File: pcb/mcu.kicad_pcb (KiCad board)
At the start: 2 copper layers, 40 x 27.1 mm, 11 parts, among them J700 Conn_01x20, J701 BL_CONN, SW700 ON_OFF, U700 xiao-ble, U701 PCA9555PW

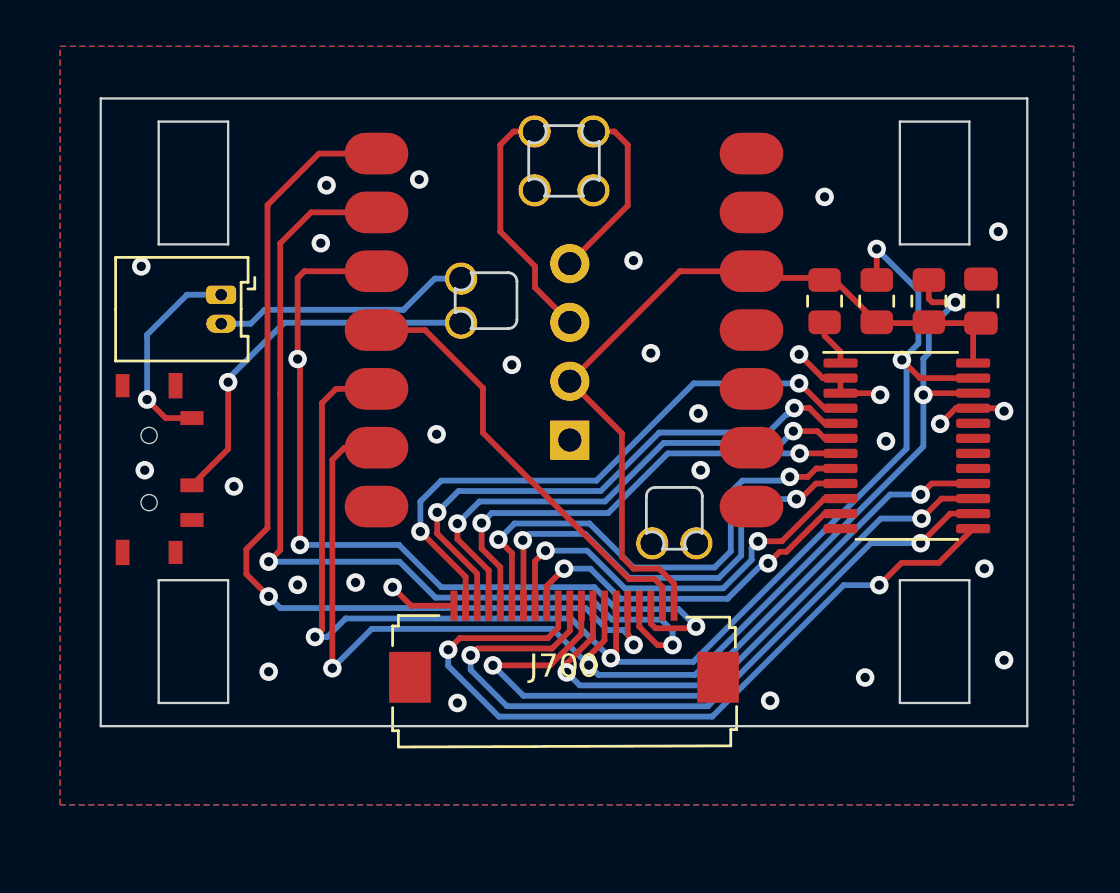
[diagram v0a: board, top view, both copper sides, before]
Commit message: Added interrupt lines and GPIO breakout
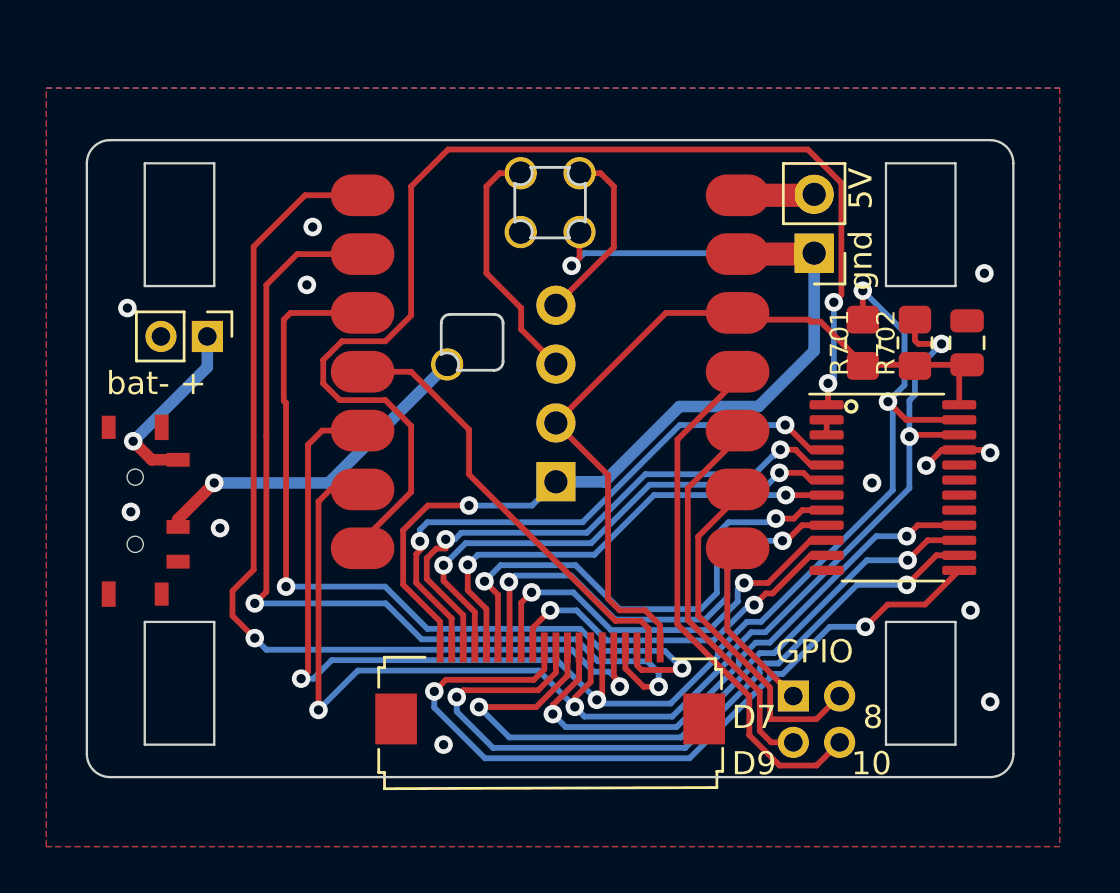
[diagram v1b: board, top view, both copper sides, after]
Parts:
- removed R700: 10k, Resistor_SMD:R_0805_2012Metric
- added J1: Conn_01x04, Connector_PinHeader_2.00mm:PinHeader_2x02_P2.00mm_Horizontal, F.Cu at (144.5, 109.0)
- added J702: Conn_01x02, Connector_PinHeader_2.54mm:PinHeader_1x02_P2.54mm_Vertical, F.Cu at (145.4, 89.9)
- R701, R702: footprint Resistor_SMD:R_0805_2012Metric -> Resistor_SMD:R_0805_2012Metric_Pad1.20x1.40mm_HandSolder
- bat- +: renamed from BT700; footprint Connector_Molex:Molex_PicoBlade_53048-0210_1x02_P1.25mm_Horizontal -> Connector_PinHeader_2.00mm:PinHeader_1x02_P2.00mm_Vertical
- moved SW700 1.90 mm to (114.7, 101.0)
- moved C700 1.90 mm to (152.0, 93.8)
- moved J700 1.90 mm to (134.0, 110.0)
- moved J701 1.90 mm to (134.2, 99.8)
- moved R701 1.90 mm to (147.5, 93.8)
- moved R702 1.90 mm to (149.8, 93.8)
- moved U700 1.90 mm to (134.0, 95.0)
- moved U701 1.90 mm to (148.8, 100.0)
- moved bat- + 1.90 mm to (119.2, 93.5)
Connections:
- U700 pad 10: unconnected-(U2-Pad10) -> D9
- U700 pad 11: unconnected-(U2-Pad11) -> D10
- U700 pad 14: unconnected-(U2-Pad14) -> +5V
- U700 pad 7: unconnected-(U2-Pad7) -> ~{int}
- U700 pad 8: unconnected-(U2-Pad8) -> D7
- U700 pad 9: unconnected-(U2-Pad9) -> D8
- U701 pad 1: Net-(R1-Pad2) -> ~{int}
- bat- + pad 2: Net-(BT1-Pad2) -> GND
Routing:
- net ~{int}: track 0.00 -> 51.8 mm, vias 0 -> 2
- net GND: track 10.7 -> 49.8 mm, vias 28 -> 14
- net D10: track 0.00 -> 23.2 mm
- net D9: track 0.00 -> 17.1 mm
- net D8: track 0.00 -> 15.6 mm
- net Net-(BT1-Pad2): track 11.2 -> 0.00 mm
- net D7: track 0.00 -> 7.94 mm
- net +5V: track 0.00 -> 2.85 mm
- net Net-(R1-Pad2): track 2.05 -> 0.00 mm
- net Net-(U700-BAT): track 16.3 -> 14.7 mm
- net Net-(BT700-+): track 8.98 -> 8.12 mm
- net Row_3: vias 3 -> 2
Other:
- board size 40 x 27.1 mm -> 40 x 27.5 mm
- board text added: "10"
- board text added: "5V"
- board text added: "8"
- board text added: "D7"
- board text added: "D9"
- board text added: "GPIO"
- board text added: "gnd"
